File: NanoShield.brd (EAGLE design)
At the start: 69.8 x 83.5 mm, 17 parts, among them K1 G5L, K2 G5L, M1 ARDUINO-NANO-3.0, M2 WIRELESS-NRF24L01, T1 2N3904, T2 2N3904

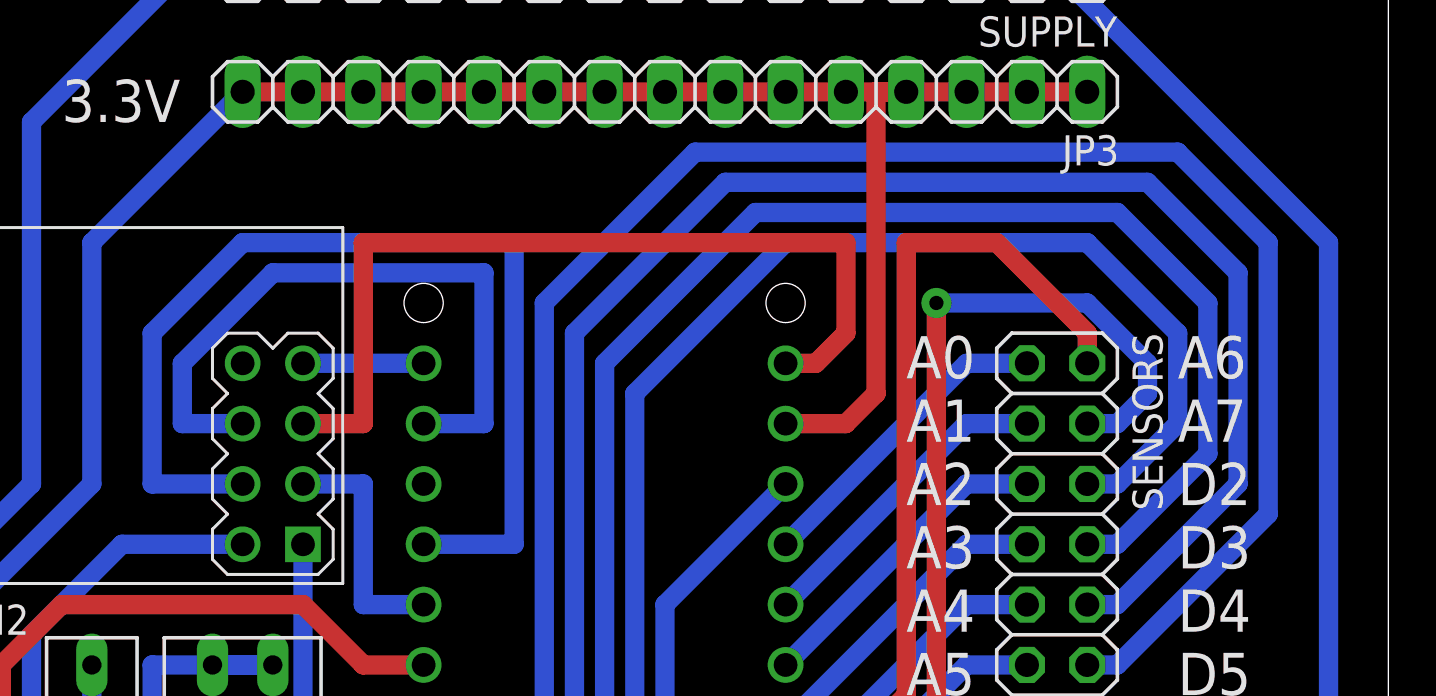
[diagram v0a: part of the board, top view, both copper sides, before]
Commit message: Fixed missing interrupt pin.
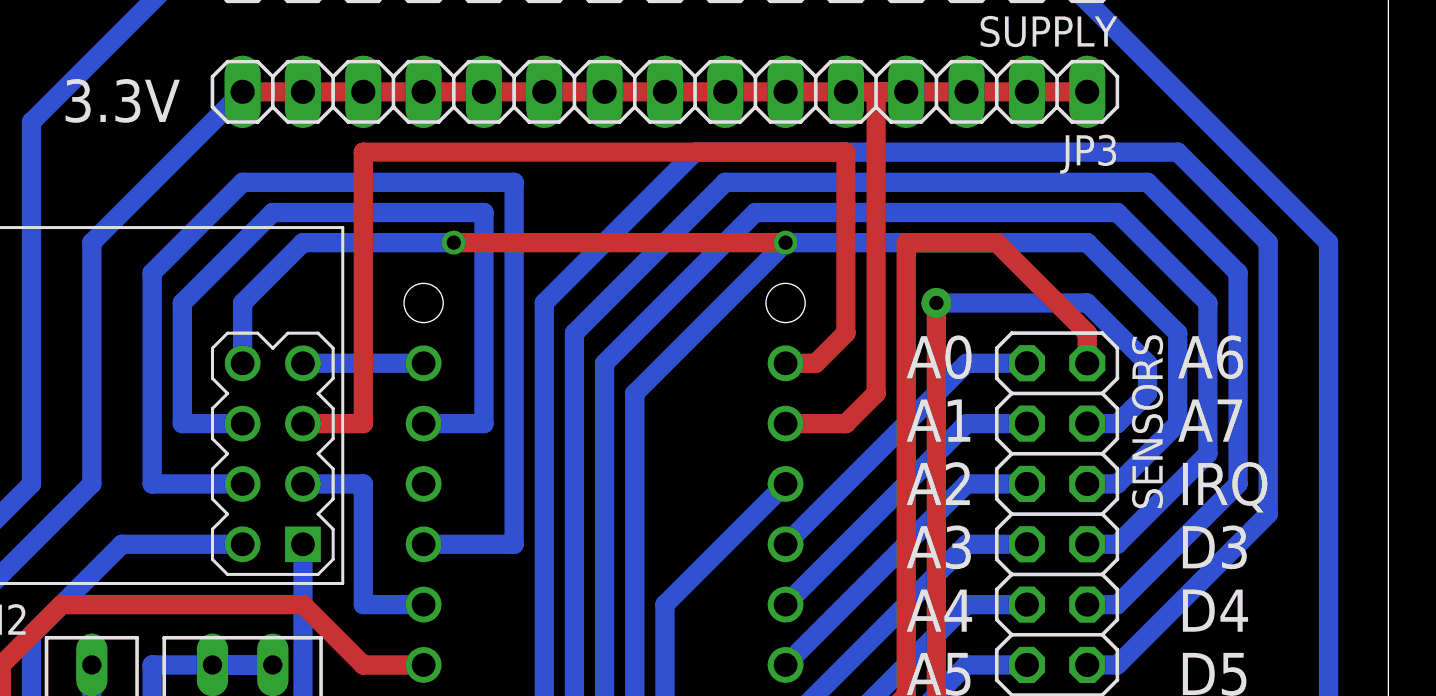
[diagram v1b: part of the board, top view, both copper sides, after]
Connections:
- net D2: now also M2.8
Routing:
- net D2: track 65.0 -> 91.5 mm, vias 0 -> 2
- net N$1: track 37.4 -> 45.0 mm
- net N$2: track 28.2 -> 33.3 mm
- net N$7: track 43.5 -> 48.6 mm
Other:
- board text added: "A6 A7 IRQ D3 D4 D5"
- board text removed: "A6 A7 D2 D3 D4 D5"
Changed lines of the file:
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@@
 <text x="73.66" y="46.99" size="1.778" layer="21">A6
 A7
-D2
+IRQ
 D3
 D4
@@
 <contactref element="M1" pad="J2.15"/>
 <contactref element="M2" pad="5"/>
-<wire x1="59.69" y1="66.04" x2="39.37" y2="66.04" width="0.8128" layer="1"/>
-<wire x1="39.37" y1="66.04" x2="39.37" y2="58.42" width="0.8128" layer="1"/>
+<wire x1="59.69" y1="69.85" x2="39.37" y2="69.85" width="0.8128" layer="1"/>
+<wire x1="39.37" y1="69.85" x2="39.37" y2="58.42" width="0.8128" layer="1"/>
 <wire x1="39.37" y1="58.42" x2="36.83" y2="58.42" width="0.8128" layer="1"/>
-<wire x1="59.69" y1="66.04" x2="59.69" y2="62.23" width="0.8128" layer="1"/>
+<wire x1="59.69" y1="69.85" x2="59.69" y2="62.23" width="0.8128" layer="1"/>
 <wire x1="59.69" y1="62.23" x2="58.42" y2="60.96" width="0.8128" layer="1"/>
 <wire x1="58.42" y1="60.96" x2="57.15" y2="60.96" width="0.8128" layer="1"/>
@@
 <contactref element="M1" pad="J1.14"/>
 <wire x1="34.29" y1="58.42" x2="31.75" y2="58.42" width="0.8128" layer="16"/>
-<wire x1="44.45" y1="64.77" x2="44.45" y2="58.42" width="0.8128" layer="16"/>
+<wire x1="44.45" y1="67.31" x2="44.45" y2="58.42" width="0.8128" layer="16"/>
 <wire x1="44.45" y1="58.42" x2="41.91" y2="58.42" width="0.8128" layer="16"/>
-<wire x1="44.45" y1="64.77" x2="35.56" y2="64.77" width="0.8128" layer="16"/>
-<wire x1="35.56" y1="64.77" x2="31.75" y2="60.96" width="0.8128" layer="16"/>
-<wire x1="31.75" y1="60.96" x2="31.75" y2="58.42" width="0.8128" layer="16"/>
+<wire x1="44.45" y1="67.31" x2="35.56" y2="67.31" width="0.8128" layer="16"/>
+<wire x1="31.75" y1="58.42" x2="31.75" y2="63.5" width="0.8128" layer="16"/>
+<wire x1="31.75" y1="63.5" x2="35.56" y2="67.31" width="0.8128" layer="16"/>
 </signal>
 <signal name="N$3">
@@
 <wire x1="44.45" y1="35.56" x2="41.91" y2="35.56" width="0.8128" layer="16"/>
 <wire x1="69.85" y1="66.04" x2="57.15" y2="66.04" width="0.8128" layer="16"/>
-<wire x1="57.15" y1="66.04" x2="50.8" y2="59.69" width="0.8128" layer="16"/>
 <wire x1="50.8" y1="59.69" x2="50.8" y2="41.91" width="0.8128" layer="16"/>
 <wire x1="69.85" y1="55.88" x2="71.12" y2="55.88" width="0.8128" layer="16"/>
@@
 <wire x1="73.66" y1="58.42" x2="73.66" y2="62.23" width="0.8128" layer="16"/>
 <wire x1="73.66" y1="62.23" x2="69.85" y2="66.04" width="0.8128" layer="16"/>
+<contactref element="M2" pad="8"/>
+<wire x1="36.83" y1="66.04" x2="43.18" y2="66.04" width="0.8128" layer="16"/>
+<via x="43.18" y="66.04" extent="1-16" drill="0.6" shape="square"/>
+<wire x1="43.18" y1="66.04" x2="57.15" y2="66.04" width="0.8128" layer="1"/>
+<via x="57.15" y="66.04" extent="1-16" drill="0.6" shape="square"/>
+<wire x1="50.8" y1="59.69" x2="57.15" y2="66.04" width="0.8128" layer="16"/>
+<wire x1="34.29" y1="60.96" x2="34.29" y2="63.5" width="0.8128" layer="16"/>
+<wire x1="34.29" y1="63.5" x2="36.83" y2="66.04" width="0.8128" layer="16"/>
 </signal>
 <signal name="D3">
@@
 <contactref element="M1" pad="J1.12"/>
 <wire x1="41.91" y1="53.34" x2="45.72" y2="53.34" width="0.8128" layer="16"/>
-<wire x1="45.72" y1="53.34" x2="45.72" y2="66.04" width="0.8128" layer="16"/>
+<wire x1="45.72" y1="53.34" x2="45.72" y2="68.58" width="0.8128" layer="16"/>
 <wire x1="30.48" y1="55.88" x2="34.29" y2="55.88" width="0.8128" layer="16"/>
-<wire x1="45.72" y1="66.04" x2="34.29" y2="66.04" width="0.8128" layer="16"/>
-<wire x1="34.29" y1="66.04" x2="30.48" y2="62.23" width="0.8128" layer="16"/>
-<wire x1="30.48" y1="62.23" x2="30.48" y2="55.88" width="0.8128" layer="16"/>
+<wire x1="45.72" y1="68.58" x2="34.29" y2="68.58" width="0.8128" layer="16"/>
+<wire x1="30.48" y1="64.77" x2="30.48" y2="55.88" width="0.8128" layer="16"/>
+<wire x1="30.48" y1="64.77" x2="34.29" y2="68.58" width="0.8128" layer="16"/>
 </signal>
 <signal name="N$11">
